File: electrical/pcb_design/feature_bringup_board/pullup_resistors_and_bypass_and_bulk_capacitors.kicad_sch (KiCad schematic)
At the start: 21 parts

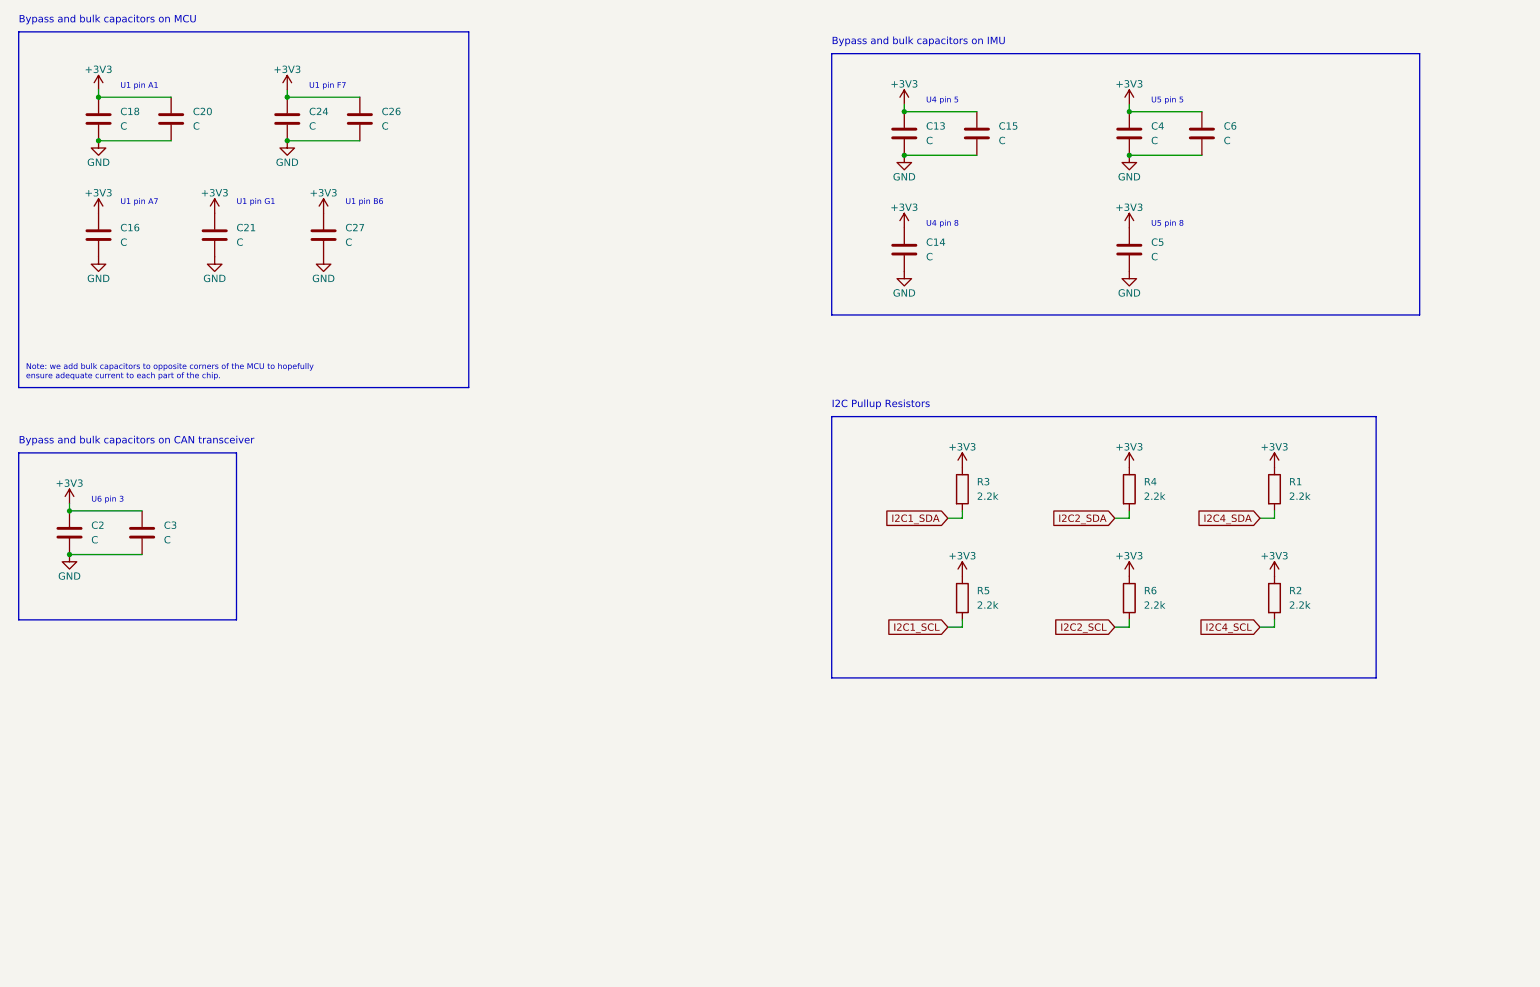
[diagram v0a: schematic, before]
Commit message: First pass on feature bringup board. All tests passing.
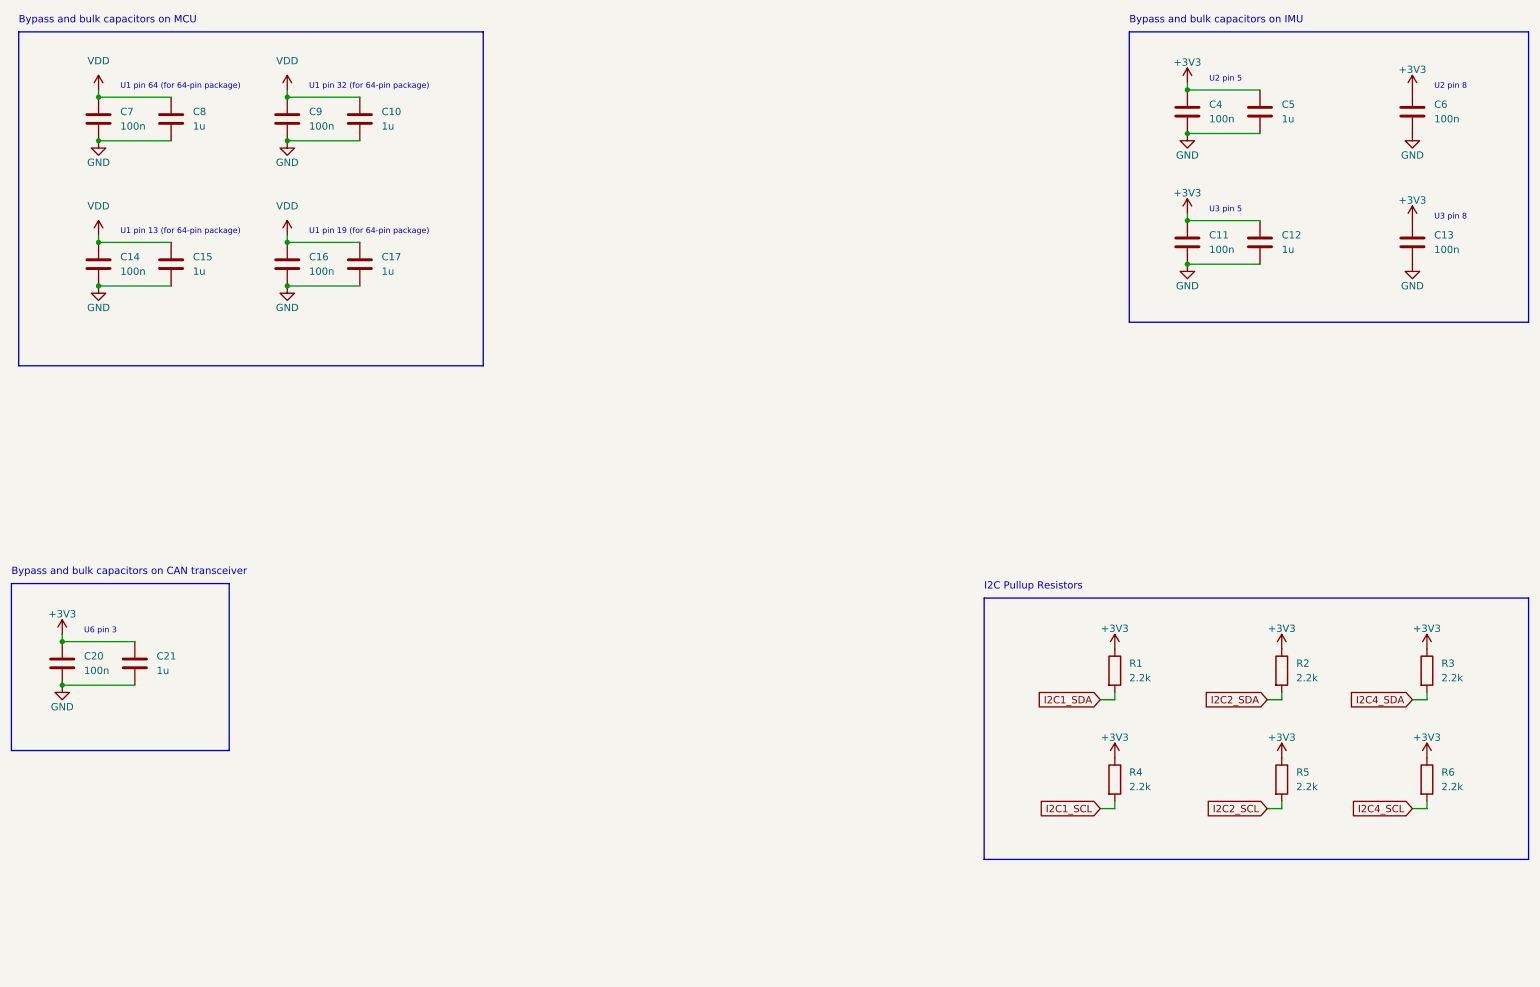
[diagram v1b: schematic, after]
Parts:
- removed C21, C27: C, symbol Device:C
- added C14: 100n, footprints:Nondescript_C_0402_1005Metric, symbol Device:C
- added C15, C17: 1u, footprints:Nondescript_C_0603_1608Metric, symbol Device:C
- C10: renamed from C26; value C -> 1u; footprint (none) -> footprints:Nondescript_C_0603_1608Metric
- C11: renamed from C4; value C -> 100n; footprint (none) -> footprints:Nondescript_C_0402_1005Metric
- C12: renamed from C6; value C -> 1u; footprint (none) -> footprints:Nondescript_C_0603_1608Metric
- C13: renamed from C5; value C -> 100n; footprint (none) -> footprints:Nondescript_C_0402_1005Metric
- C16: value C -> 100n; footprint (none) -> footprints:Nondescript_C_0402_1005Metric
- C20: renamed from C2; value C -> 100n; footprint (none) -> footprints:Nondescript_C_0402_1005Metric
- C21: renamed from C3; value C -> 1u; footprint (none) -> footprints:Nondescript_C_0603_1608Metric
- C4: renamed from C13; value C -> 100n; footprint (none) -> footprints:Nondescript_C_0402_1005Metric
- C5: renamed from C15; value C -> 1u; footprint (none) -> footprints:Nondescript_C_0603_1608Metric
- C6: renamed from C14; value C -> 100n; footprint (none) -> footprints:Nondescript_C_0402_1005Metric
- C7: renamed from C18; value C -> 100n; footprint (none) -> footprints:Nondescript_C_0402_1005Metric
- C8: renamed from C20; value C -> 1u; footprint (none) -> footprints:Nondescript_C_0603_1608Metric
- C9: renamed from C24; value C -> 100n; footprint (none) -> footprints:Nondescript_C_0402_1005Metric
- renumbered R3 to R1, R4 to R2, R1 to R3, R5 to R4, R6 to R5, R2 to R6
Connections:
- net +3V3: no longer C10.1, C16.1, C7.1, C8.1, C9.1
- net GND: now also C14.2, C15.2, C17.2
- new net VDD: C10.1, C14.1, C15.1, C16.1, C17.1, C7.1, C8.1, C9.1
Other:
- note added: "U1 pin 13 (for 64-pin package)"
- note added: "U1 pin 19 (for 64-pin package)"
- note added: "U1 pin 32 (for 64-pin package)"
- note added: "U1 pin 64 (for 64-pin package)"
- note added: "U2 pin 5"
- note added: "U2 pin 8"
- note added: "U3 pin 5"
- note added: "U3 pin 8"
- note removed: "Note: we add bulk capacitors to opposite corners of the MCU to hopefully ensure adequate current to each part of the chip."
- note removed: "U1 pin A1"
- note removed: "U1 pin A7"
- note removed: "U1 pin B6"
- note removed: "U1 pin F7"
- note removed: "U1 pin G1"
- note removed: "U4 pin 5"
- note removed: "U4 pin 8"
- note removed: "U5 pin 5"
- note removed: "U5 pin 8"
- moved on the sheet: C11, C12, C13, C20, C21, C4, C5, C6, R1, R2, R3, R4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

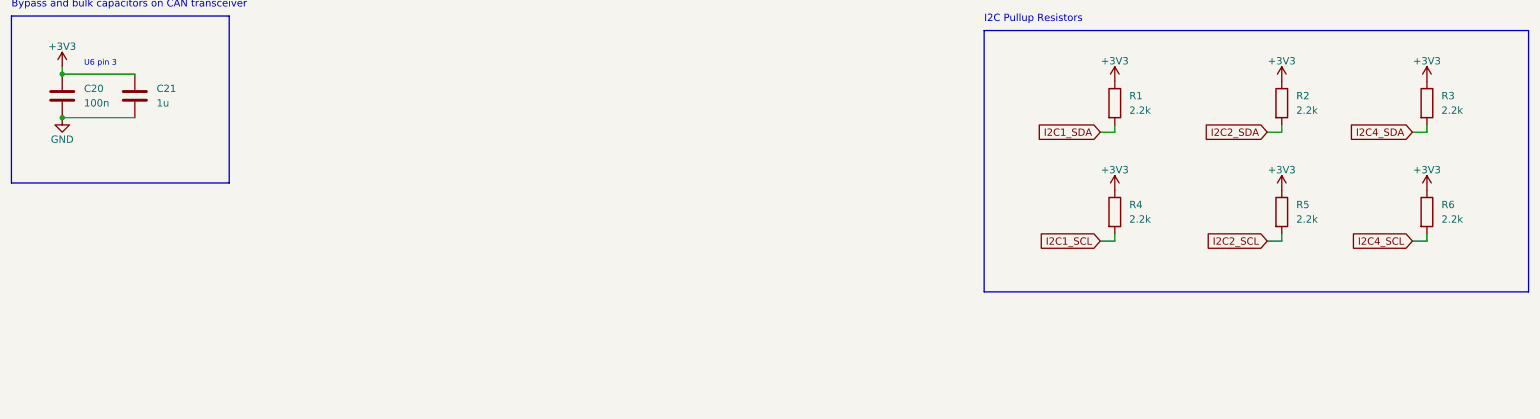
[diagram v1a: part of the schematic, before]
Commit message: Misc tweaks and fixes, including adding bypass capacitors on power monitors, finalizing most part selections, and tweaking track layouts.
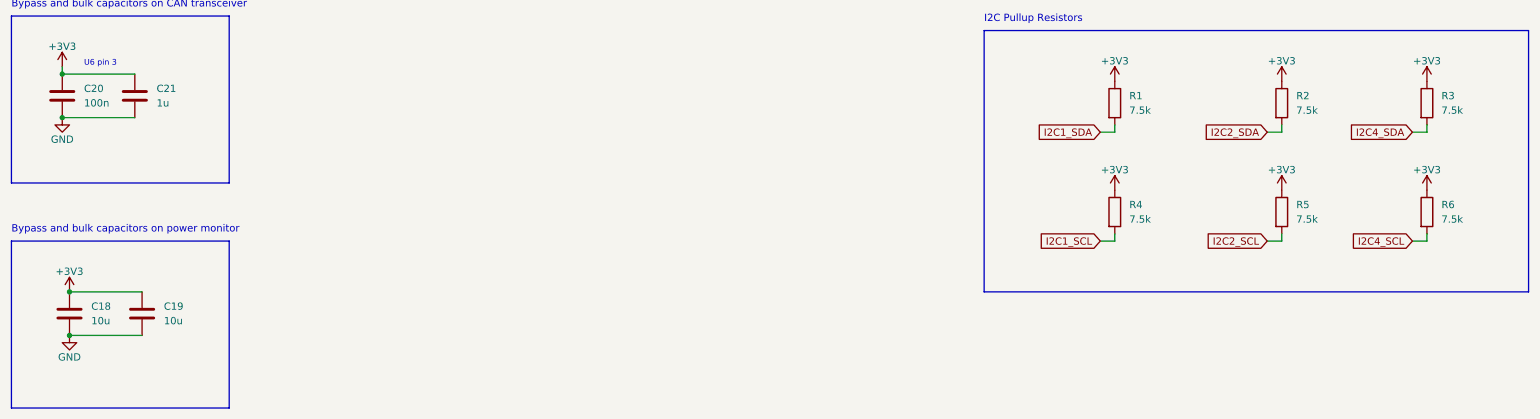
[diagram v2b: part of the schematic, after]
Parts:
- added C18, C19: 10u, footprints:Nondescript_C_0603_1608Metric, symbol Device:C
- C10, C12, C15, C17, C21, C5, C8: Active (none) -> Y; MPN (none) -> C77046; Manufacturer (none) -> Murata Electronics; Manufacturer Part Number (none) -> GRM188R61E105KA12D
- C11, C13, C14, C16, C20, C4, C6, C7, C9: Active (none) -> Y; MPN (none) -> C77014; Manufacturer (none) -> Murata Electronics; Manufacturer Part Number (none) -> GRM155R71E104KE14D
- R1, R2, R3, R4, R5, R6: value 2.2k -> 7.5k; footprint Resistor_SMD:R_0402_1005Metric -> footprints:Nondescript_R_0402_1005Metric; Active (none) -> Y; MPN C517529 -> C137934; Manufacturer UNI-ROYAL(Uniroyal Elec) -> YAGEO; Manufacturer Part Number TC0250D2201TCC -> RC0402FR-077K5L
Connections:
- net +3V3: now also C18.1, C19.1
- net GND: now also C18.2, C19.2
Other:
- note added: "Bypass and bulk capacitors on power monitor"

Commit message: Added silkscreening to thank the Hacker Initiative
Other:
- company: (none) -> TVSC
- title: (none) -> Feature Bringup Board
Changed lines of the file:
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@@
 (kicad_sch (version 20230121) (generator eeschema)
-  (paper "A4")
+  (paper "USLetter")
+  (title_block
+    (title "Feature Bringup Board")
+    (date "2025-02-12")
+    (rev "${PCB_VERSION}")
+    (company "TVSC")
+  )
   (junction (at 222.25 29.21) (diameter 0) (color 0 0 0 0)
   )
